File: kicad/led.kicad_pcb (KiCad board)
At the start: 2 copper layers, 7 parts, among them J1 INPUT, J2 OUTPUT, Q1 Q_NMOS_DGS, SW1 SW DOWN, SW2 SW UP, U1 PIC10F200-IP

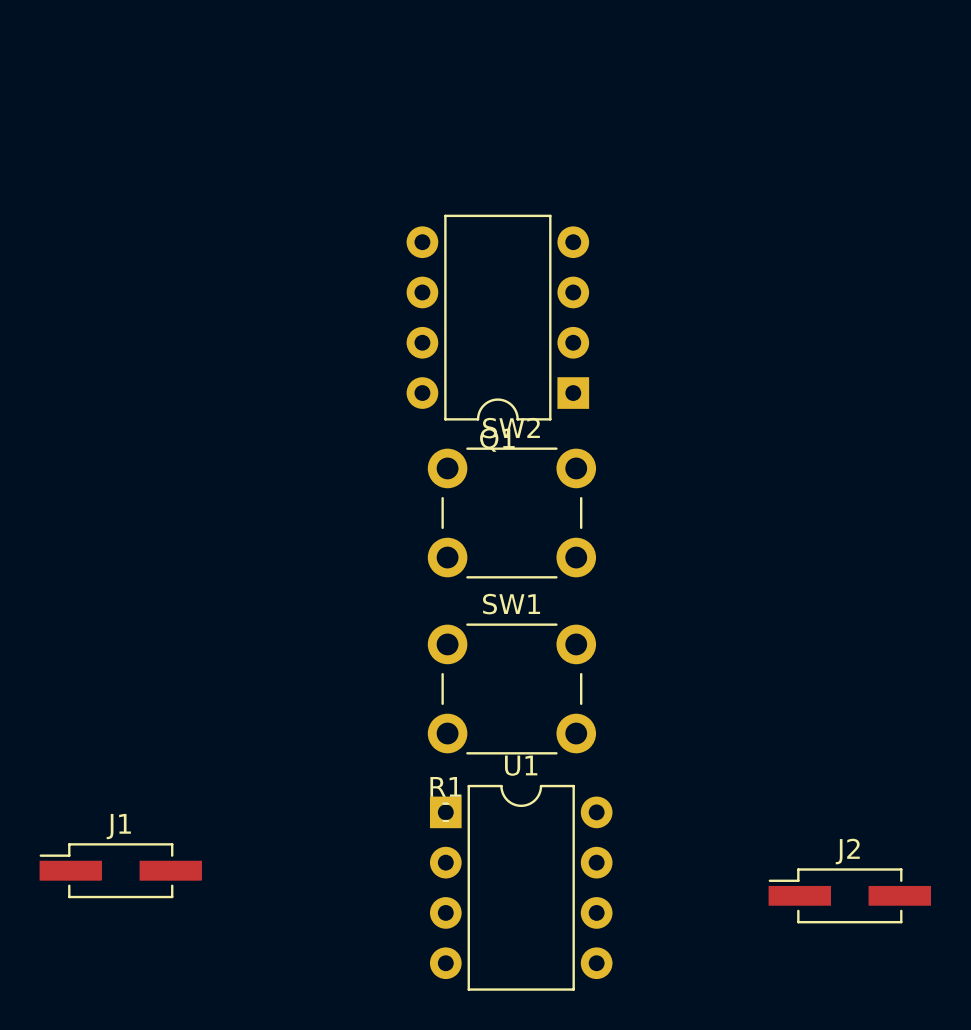
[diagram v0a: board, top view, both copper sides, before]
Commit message: Added a diode to isolate "power" VDD to microcontroler VDD. Changed some footprints to enable bigger resistor and capacitor. Moved a bit the headers in order to fit. Added extra soldering pads to VIN an VOUT in order to allow soldering the wires directly, instead of using headers. Some other small changes.
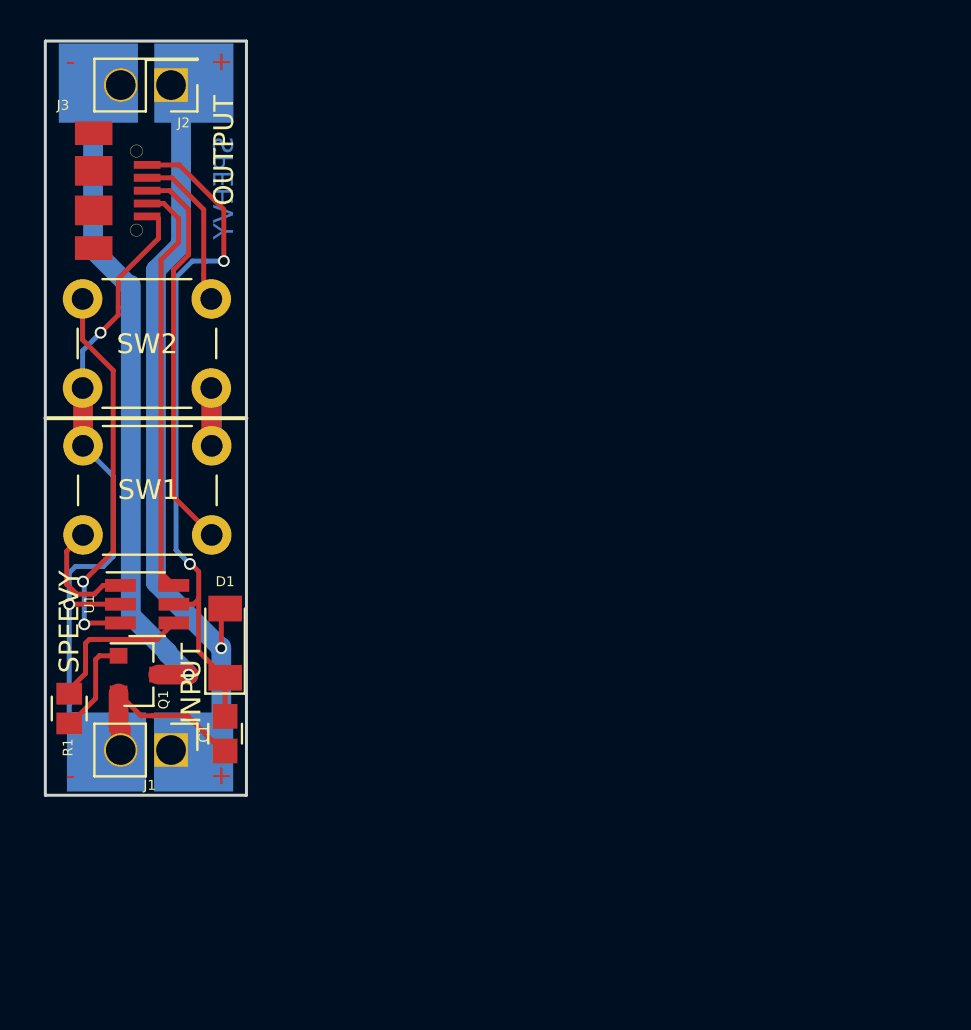
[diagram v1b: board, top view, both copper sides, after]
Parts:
- added C1: 100nF, Capacitors_SMD:C_0805, F.Cu at (137.4, 101.0)
- added D1: 1N4148, Diodes_SMD:D_MiniMELF, F.Cu at (137.4, 96.5)
- added J3: USB_OTG, Connectors_USB:USB_Micro-B_Molex-105017-0001, F.Cu at (131.1, 73.6)
- J1: footprint Pin_Headers:Pin_Header_Straight_2x01_Pitch2.54mm_SMD -> Pin_Headers:Pin_Header_Straight_1x02_Pitch2.54mm
- J2: footprint Pin_Headers:Pin_Header_Straight_2x01_Pitch2.54mm_SMD -> Pin_Headers:Pin_Header_Straight_2x01_Pitch2.54mm
- Q1: value Q_NMOS_DGS -> SI2306; footprint Housings_DIP:DIP-8_W7.62mm -> TO_SOT_Packages_SMD:SOT-23
- R1: footprint Resistors_SMD:R_0201 -> Resistors_SMD:R_0805
- U1: footprint Housings_DIP:DIP-8_W7.62mm -> TO_SOT_Packages_SMD:SOT-23-6_Handsoldering
- moved J2 53.4 mm to (134.6, 68.3), turned to 180 degrees
- moved Q1 26.2 mm to (133.0, 98.0), turned to 0 degrees
- moved SW1 21.0 mm to (130.2, 86.5)
- moved R1 19.7 mm to (129.5, 99.8), turned to 90 degrees
- moved U1 18.4 mm to (133.4, 94.5)
- moved SW2 12.6 mm to (136.7, 83.6), turned to 180 degrees
- moved J1 6.60 mm to (134.6, 101.9), turned to 270 degrees
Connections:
- Q1 pad 1: Net-(J2-Pad2) -> Net-(Q1-Pad1)
- Q1 pad 2: Net-(Q1-Pad2) -> GNDD
- Q1 pad 3: GNDD -> Net-(Q1-Pad3)
- R1 pad 1: Net-(Q1-Pad2) -> Net-(Q1-Pad1)
- SW1 pad 2: Net-(SW1-Pad2) -> Net-(J3-Pad3)
- SW2 pad 2: Net-(SW2-Pad2) -> Net-(J3-Pad2)
- U1 pad 1: (no net) -> Net-(J3-Pad3)
- U1 pad 2: VDD -> GNDD
- U1 pad 3: Net-(R1-Pad2) -> Net-(J3-Pad2)
- U1 pad 4: Net-(SW2-Pad2) -> Net-(R1-Pad2)
- U1 pad 5: Net-(SW1-Pad2) -> Net-(C1-Pad2)
- U1 pad 6: (no net) -> Net-(J3-Pad4)
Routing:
- net GNDD: track 0.00 -> 50.6 mm, vias 0 -> 2
- net VDD: track 0.00 -> 40.4 mm, vias 0 -> 1
- net Net-(C1-Pad2): track 0.00 -> 34.6 mm, vias 0 -> 2
- net Net-(Q1-Pad3): track 0.00 -> 34.3 mm, vias 0 -> 1
- net Net-(J3-Pad2): track 0.00 -> 27.8 mm, vias 0 -> 2
- net Net-(J3-Pad3): track 0.00 -> 26.1 mm
- net Net-(J3-Pad4): track 0.00 -> 21.9 mm
- net Net-(R1-Pad2): track 0.00 -> 7.58 mm
- net Net-(Q1-Pad1): track 0.00 -> 5.23 mm
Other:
- board outline added: 10.2 x 38.1 mm
- net class power added: clearance 0.2, trace_width 1.27, via_dia 0.6, via_drill 0.4
- board text added: "+"
- board text added: "-"
- board text added: "SPEEVY"

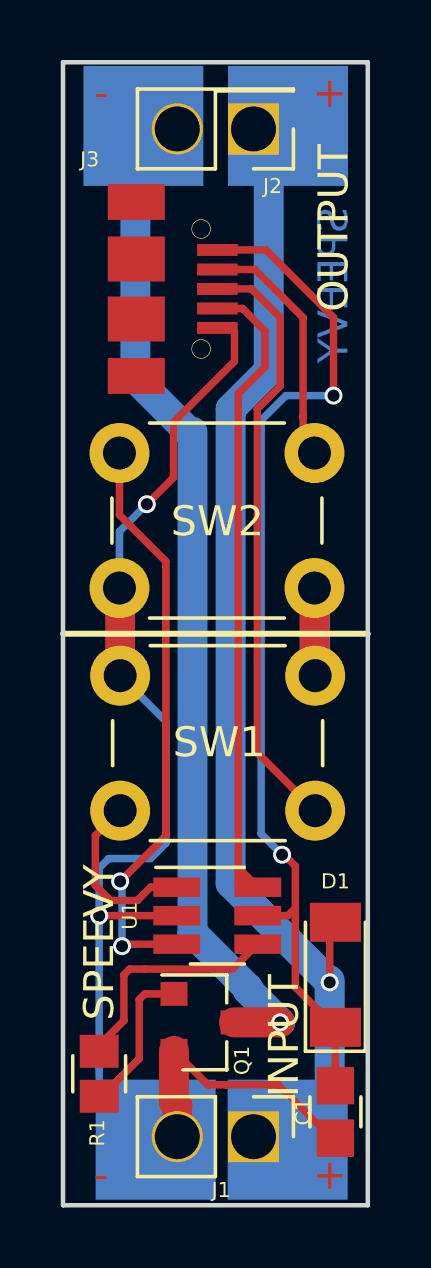
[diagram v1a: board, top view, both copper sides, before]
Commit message: Modified to allow input voltages > 5V. Also removed micro usb connector for programming, and added some test points in its place.
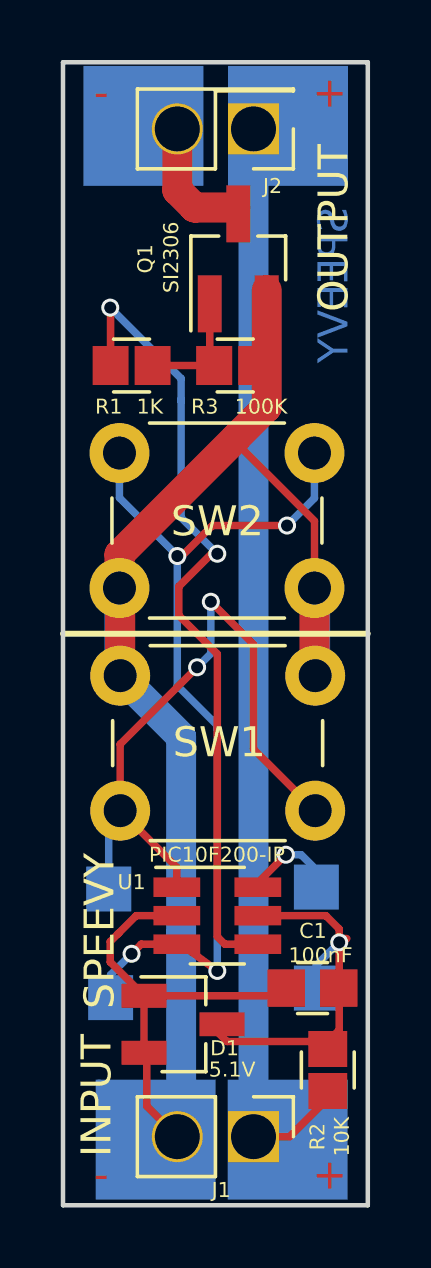
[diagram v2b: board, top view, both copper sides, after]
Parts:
- added J4: VPP (1), Measurement_Points:Measurement_Point_Square-SMD-Pad_Small, B.Cu at (136.7, 93.5)
- added J5: DAT (4), Measurement_Points:Measurement_Point_Square-SMD-Pad_Small, B.Cu at (129.8, 93.6)
- added J6: CLK (5), Measurement_Points:Measurement_Point_Square-SMD-Pad_Small, B.Cu at (129.9, 97.2)
- added R2: 10K, Resistors_SMD:R_0805, F.Cu at (137.1, 99.6)
- added R3: 100K, Resistors_SMD:R_0805, F.Cu at (134.0, 76.1)
- D1: value 1N4148 -> 5.1V; footprint Diodes_SMD:D_MiniMELF -> Diodes_SMD:D_SOT-23_ANK
- J3: value USB_OTG -> VDD (2); footprint Connectors_USB:USB_Micro-B_Molex-105017-0001 -> Measurement_Points:Measurement_Point_Square-SMD-Pad_Small; moved to B.Cu
- Q1: footprint TO_SOT_Packages_SMD:SOT-23 -> TO_SOT_Packages_SMD:SOT-23_Handsoldering
- R1: value 10K -> 1K
- moved Q1 25.5 mm to (134.1, 72.6), turned to 90 degrees
- moved J3 24.0 mm to (136.7, 96.9), turned to 0 degrees
- moved R1 23.6 mm to (130.6, 76.1), turned to 180 degrees
- moved D1 5.34 mm to (132.3, 98.1), turned to 0 degrees
- moved C1 4.20 mm to (136.6, 96.9), turned to 0 degrees
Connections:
- D1 pad 2: VDD -> GNDD
- Q1 pad 3: Net-(Q1-Pad3) -> Net-(J2-Pad2)
- SW1 pad 2: Net-(J3-Pad3) -> Net-(J5-Pad1)
- SW2 pad 2: Net-(J3-Pad2) -> Net-(J6-Pad1)
- U1 pad 1: Net-(J3-Pad3) -> Net-(J5-Pad1)
- U1 pad 3: Net-(J3-Pad2) -> Net-(J6-Pad1)
- U1 pad 6: Net-(J3-Pad4) -> Net-(J4-Pad1)
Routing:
- net Net-(Q1-Pad3): track 34.3 -> 0.00 mm, vias 1 -> 0
- net Net-(J6-Pad1): track 0.00 -> 31.1 mm, vias 0 -> 4
- net Net-(J3-Pad2): track 27.8 -> 0.00 mm, vias 2 -> 0
- net Net-(J3-Pad3): track 26.1 -> 0.00 mm
- net Net-(J5-Pad1): track 0.00 -> 22.7 mm, vias 0 -> 2
- net Net-(J3-Pad4): track 21.9 -> 0.00 mm
- net Net-(C1-Pad2): track 34.6 -> 13.1 mm, vias 2 -> 1
- net Net-(R1-Pad2): track 7.58 -> 27.1 mm, vias 0 -> 2
- net GNDD: track 50.6 -> 66.7 mm, vias 2 -> 0
- net Net-(J2-Pad2): track 0.00 -> 7.92 mm
- net Net-(J4-Pad1): track 0.00 -> 3.29 mm, vias 0 -> 1
- net Net-(Q1-Pad1): track 5.23 -> 4.17 mm
- net VDD: track 40.4 -> 40.1 mm, vias 1 -> 0
